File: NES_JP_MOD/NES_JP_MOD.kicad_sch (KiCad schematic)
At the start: 9 parts, among them J1 Conn_01x06, U1 XC2C64A, U2 AMS1117-1.8, U3 AMS1117-3.3, X1 ASV-xxxMHz

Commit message: Created PCB
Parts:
- added C5, C6, C7, C8, C9: 0.1u, Capacitor_SMD:C_0805_2012Metric, symbol Device:C
- added Q1: MMBT3904, Package_TO_SOT_SMD:SOT-23, symbol Transistor_BJT:MMBT3904
- added R1, R12, R8: 5K6, Resistor_SMD:R_0805_2012Metric, symbol Device:R
- added R10, R11, R13, R14, R15, R16, R17, R18, R2, R3, R4, R5, R6, R7, R9: 10K, Resistor_SMD:R_0805_2012Metric, symbol Device:R
- added TP1, TP10, TP11, TP12, TP13, TP14, TP15, TP16, TP17, TP2, TP3, TP4, TP5, TP6, TP7, TP8, TP9: TestPoint, TestPoint:TestPoint_Pad_2.0x2.0mm, symbol Connector:TestPoint
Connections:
- net +3.3V is gone; now on net +3V3: C4.1, J1.1 (Pin_1), U1.3 (VAUX), U3.2 (VO), X1.4 (Vdd)
- net +1V8: now also U1.29 (Vcc), C8.1
- net +5V: now also R2.1, TP16.1
- net CLK: now also U1.1 (I/O)
- net GND: now also C5.2, C6.2, C7.2, C8.2, C9.2, Q1.2 (E), R13.2, R9.2, TP17.1
- net BTN6: now reaches U1.10 (I/O)
- net BTN6: now also R10.2, TP8.1
- net +3V3: now reaches U1.19 (Vccio1)
- net +3V3: now also U1.42 (Vccio2), C5.1, C6.1, C7.1, C9.1, R10.1, R11.1, R14.1, R15.1, R16.1, R17.1, R18.1, R3.1, R4.1, R5.1, R6.1, R7.1
- net BTN7: now reaches U1.24 (I/O)
- net BTN7: now also R7.2, TP9.1
- net BTN8: now reaches U1.25 (I/O)
- net BTN8: now also R6.2, TP10.1
- net BTN9: now reaches U1.26 (I/O)
- net BTN9: now also R5.2, TP11.1
- net BTN10: now reaches U1.27 (I/O)
- net BTN10: now also R4.2, TP12.1
- net BTN11: now reaches U1.28 (I/O)
- net BTN11: now also R3.2, TP13.1
- net LATCH_DIV: now reaches U1.34 (I/O)
- net LATCH_DIV: now also R12.2, R13.1
- net CLK_DIV: now reaches U1.35 (I/O)
- net CLK_DIV: now also R8.2, R9.1
- net DATA_Q: now reaches U1.36 (I/O)
- net DATA_Q: now also R1.1
- net BTN0: now reaches U1.4 (I/O)
- net BTN0: now also R18.2, TP2.1
- net BTN1: now reaches U1.5 (I/O)
- net BTN1: now also R17.2, TP3.1
- net BTN2: now reaches U1.6 (I/O)
- net BTN2: now also R16.2, TP4.1
- net BTN3: now reaches U1.7 (I/O)
- net BTN3: now also R15.2, TP5.1
- net BTN4: now reaches U1.8 (I/O)
- net BTN4: now also R14.2, TP6.1
- net BTN5: now reaches U1.9 (I/O)
- net BTN5: now also R11.2, TP7.1
- new net: Q1.1 (B), R1.2
- new net NES_CLK: R8.1, TP14.1
- new net NES_DATA: Q1.3 (C), R2.2, TP1.1
- new net NES_LATCH: R12.1, TP15.1
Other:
- moved on the sheet: C1, C2, C3, C4, J1, U1, U2, U3, X1

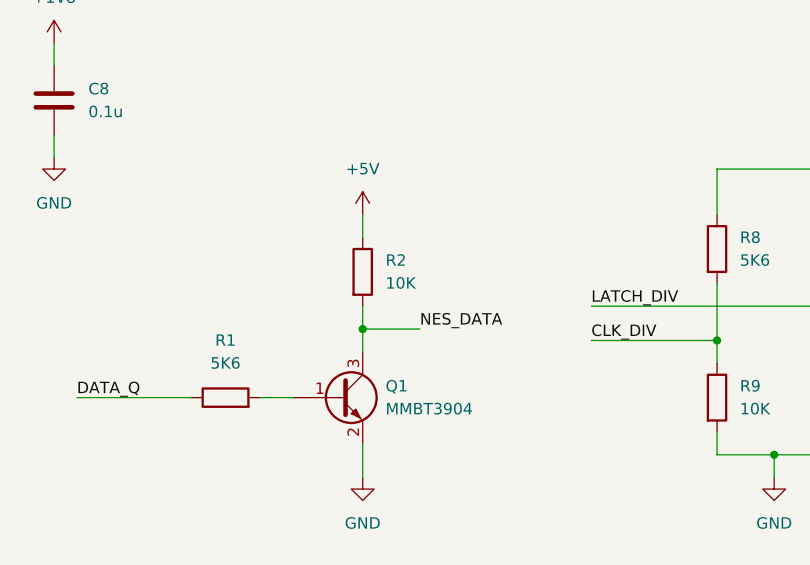
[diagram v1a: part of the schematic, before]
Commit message: Fixed wrong resistor value
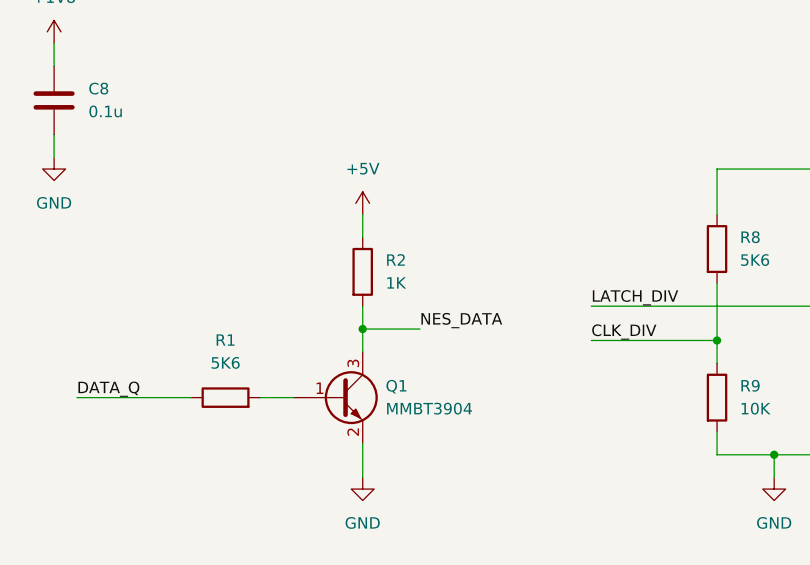
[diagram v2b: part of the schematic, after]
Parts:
- R2: value 10K -> 1K
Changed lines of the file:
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@@
       (effects (font (size 1.27 1.27)) (justify left))
     )
-    (property "Value" "10K" (id 1) (at 172.72 126.9999 0)
+    (property "Value" "1K" (id 1) (at 172.72 126.9999 0)
       (effects (font (size 1.27 1.27)) (justify left))
     )
@@
     )
     (path "/1f6631f2-60f8-4e25-baee-86413b18aefc"
-      (reference "R2") (unit 1) (value "10K") (footprint "Resistor_SMD:R_0805_2012Metric")
+      (reference "R2") (unit 1) (value "1K") (footprint "Resistor_SMD:R_0805_2012Metric")
     )
     (path "/2384dce3-62a2-4194-a7c9-d53b2a2cc920"
